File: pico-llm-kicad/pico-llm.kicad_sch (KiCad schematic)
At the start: 22 parts, among them J1 1051620001, J2 Conn_01x03_Socket, U3 AP2112K-3.3

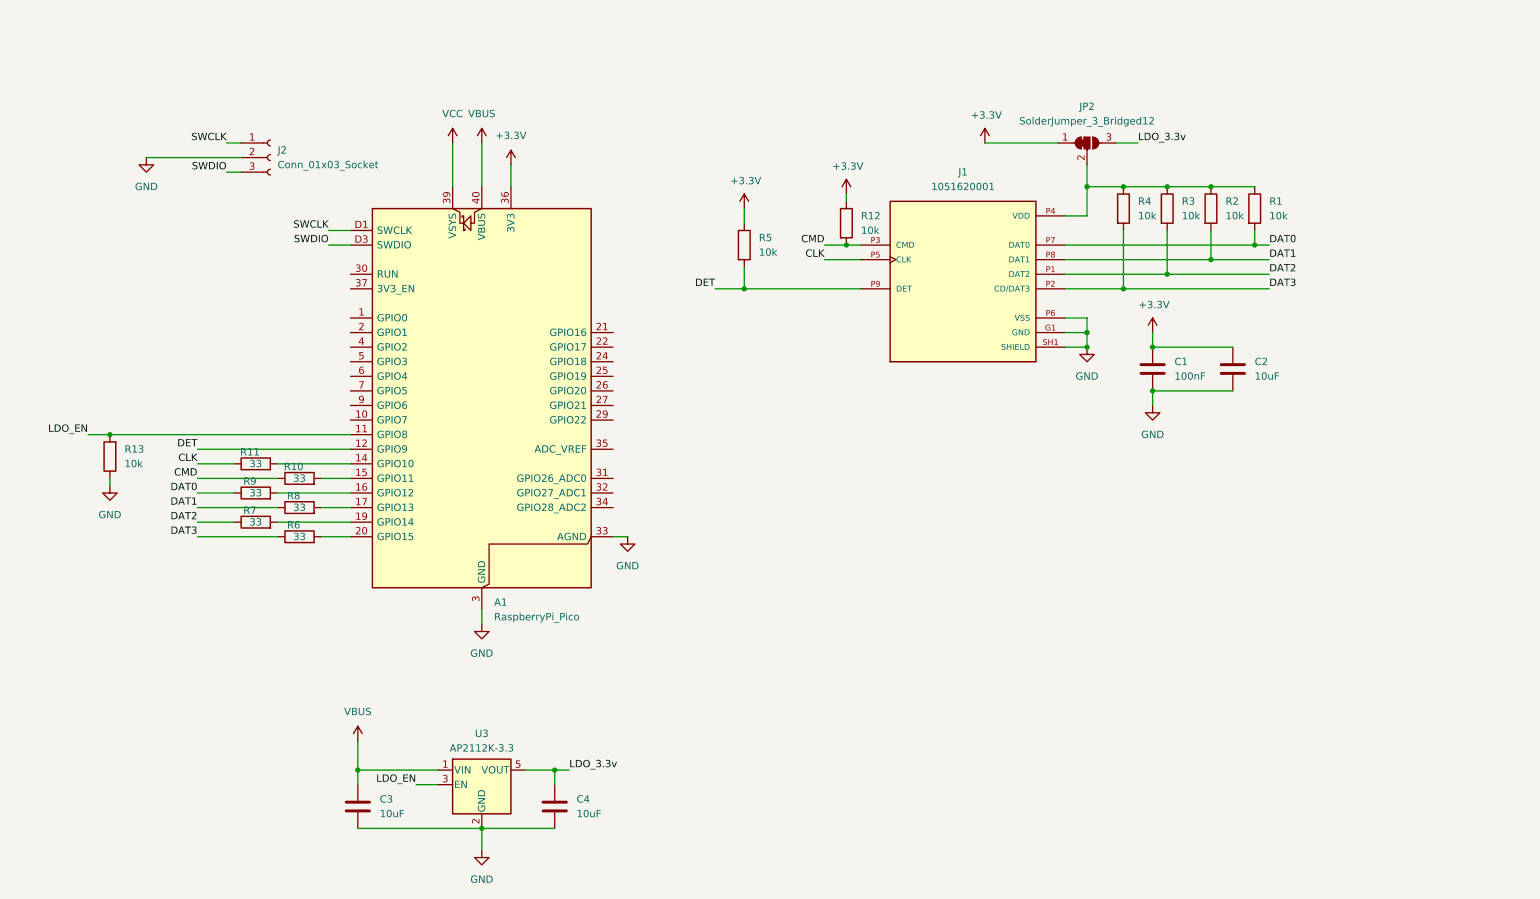
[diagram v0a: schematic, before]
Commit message: Update KiCad PCB design and add production files
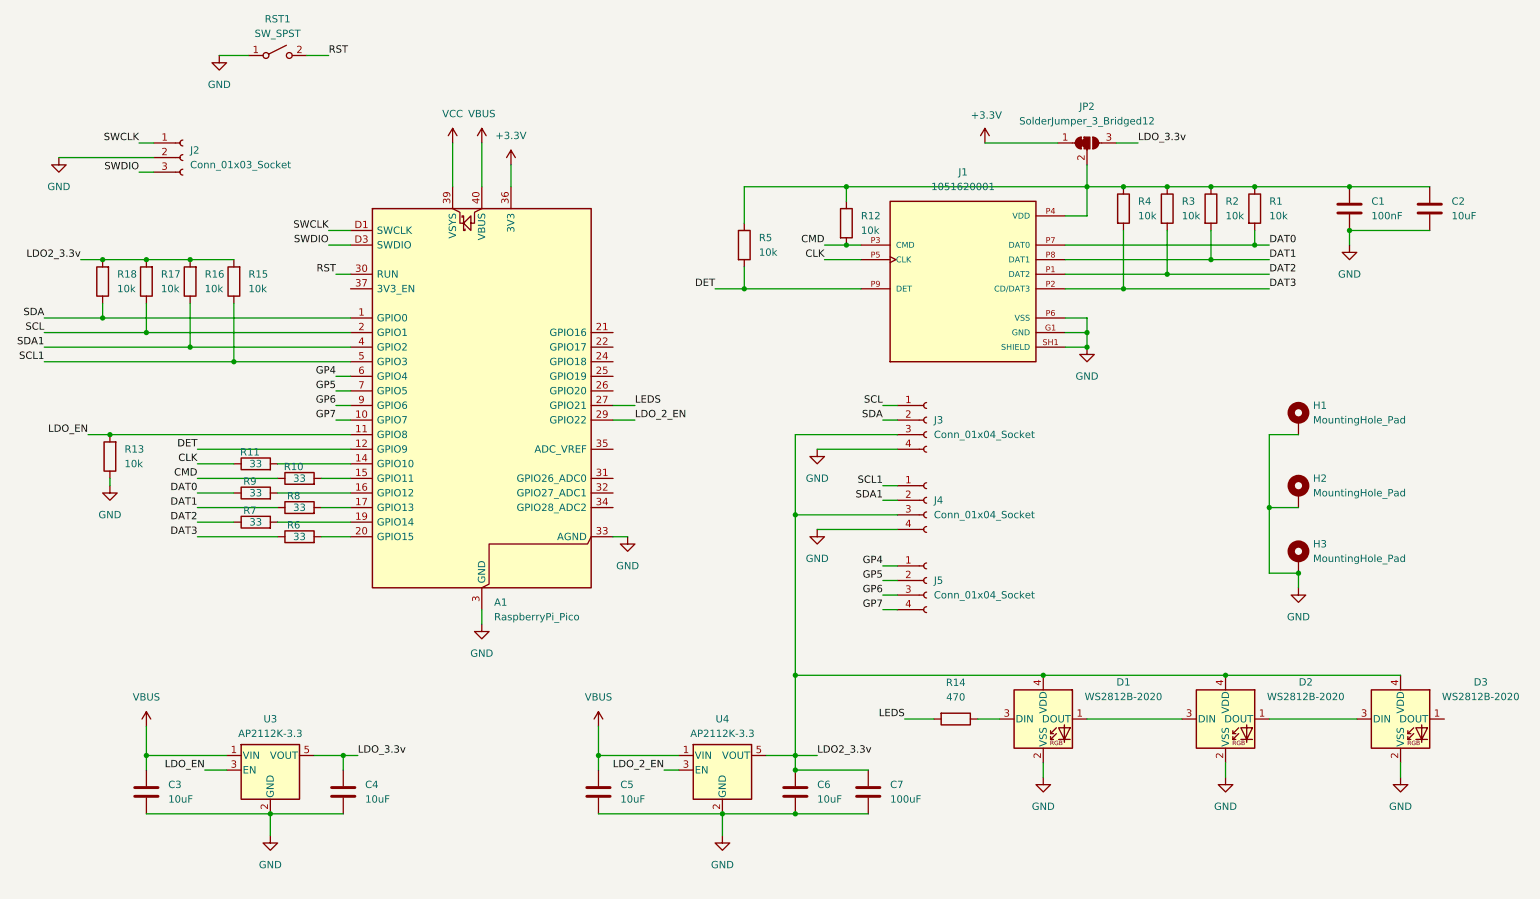
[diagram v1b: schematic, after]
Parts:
- added C5, C6: 10uF, Capacitor_SMD:C_0603_1608Metric_Pad1.08x0.95mm_HandSolder, symbol Device:C
- added C7: 100uF, Capacitor_SMD:C_1206_3216Metric_Pad1.33x1.80mm_HandSolder, symbol Device:C
- added D1, D2, D3: WS2812B-2020, LED_SMD:LED_WS2812B-2020_PLCC4_2.0x2.0mm, symbol LED:WS2812B-2020
- added H1, H2, H3: MountingHole_Pad, MountingHole:MountingHole_3.2mm_M3_Pad_TopBottom, symbol Mechanical:MountingHole_Pad
- added J3, J4, J5: Conn_01x04_Socket, Connector_JST:JST_SH_SM04B-SRSS-TB_1x04-1MP_P1.00mm_Horizontal, symbol Connector:Conn_01x04_Socket
- added R14: 470, Resistor_SMD:R_0603_1608Metric_Pad0.98x0.95mm_HandSolder, symbol Device:R
- added R15, R16, R17, R18: 10k, Resistor_SMD:R_0603_1608Metric_Pad0.98x0.95mm_HandSolder, symbol Device:R
- added RST1: SW_SPST, Button_Switch_SMD:SW_Push_1P1T-SH_NO_CK_KMR2xxG, symbol Switch:SW_SPST
- added U4: AP2112K-3.3, Package_TO_SOT_SMD:SOT-23-5, symbol Regulator_Linear:AP2112K-3.3
- J1: footprint 1051620001:MOLEX_1051620001 -> 1051620001 (1):MOLEX_1051620001
- J2: footprint Connector_PinHeader_2.54mm:PinHeader_1x03_P2.54mm_Horizontal -> Connector_JST:JST_SH_SM03B-SRSS-TB_1x03-1MP_P1.00mm_Horizontal
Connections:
- net +3.3V: no longer C1.1, C2.1, R12.1, R5.1
- net GND: now also C5.2, C6.2, C7.2, D1.2 (VSS), D2.2 (VSS), D3.2 (VSS), H1.1, H2.1, H3.1, J3.4 (Pin_4), J4.4 (Pin_4), RST1.1 (A), U4.2 (GND)
- net VBUS: now also C5.1, U4.1 (VIN)
- net at J1.P4 (VDD), JP2.2 (C), R1.1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: now also C1.1, C2.1, R12.1, R5.1
- net SDA: now reaches A1.1 (GPIO0)
- net SDA: now also J3.2 (Pin_2), R18.1
- net GP7: now reaches A1.10 (GPIO7)
- net GP7: now also J5.4 (Pin_4)
- net SCL: now reaches A1.2 (GPIO1)
- net SCL: now also J3.1 (Pin_1), R17.1
- net LEDS: now reaches A1.27 (GPIO21)
- net LEDS: now also R14.2
- net LDO_2_EN: now reaches A1.29 (GPIO22)
- net LDO_2_EN: now also U4.3 (EN)
- net RST: now reaches A1.30 (RUN)
- net RST: now also RST1.2 (B)
- net SDA1: now reaches A1.4 (GPIO2)
- net SDA1: now also J4.2 (Pin_2), R16.1
- net SCL1: now reaches A1.5 (GPIO3)
- net SCL1: now also J4.1 (Pin_1), R15.1
- net GP4: now reaches A1.6 (GPIO4)
- net GP4: now also J5.1 (Pin_1)
- net GP5: now reaches A1.7 (GPIO5)
- net GP5: now also J5.2 (Pin_2)
- net GP6: now reaches A1.9 (GPIO6)
- net GP6: now also J5.3 (Pin_3)
- new net: D1.3 (DIN), R14.1
- new net: D2.1 (DOUT), D3.3 (DIN)
- new net: D1.1 (DOUT), D2.3 (DIN)
- new net LDO2_3.3v: C6.1, C7.1, D1.4 (VDD), D2.4 (VDD), D3.4 (VDD), J3.3 (Pin_3), J4.3 (Pin_3), R15.2, R16.2, R17.2, R18.2, U4.5 (VOUT)
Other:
- moved on the sheet: C1, C2, C3, C4, J2, U3
